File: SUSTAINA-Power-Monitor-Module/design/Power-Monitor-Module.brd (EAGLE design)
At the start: 20.3 x 12.7 mm, 25 parts, among them IC1 INA226, P1 2X5P, P2 2X5P, P3 1X4P

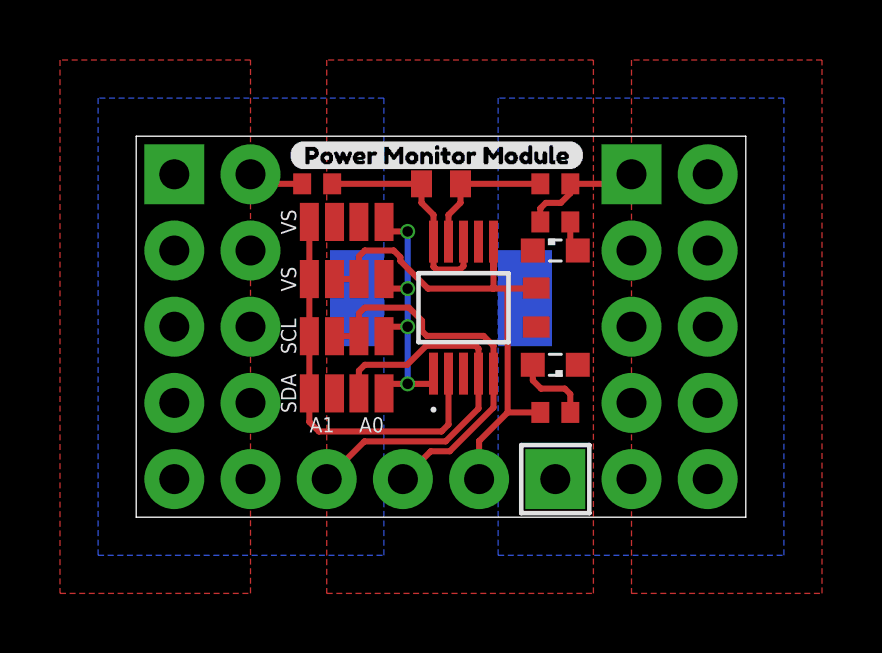
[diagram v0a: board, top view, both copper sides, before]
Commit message: Corrected the silk printing and via processing method
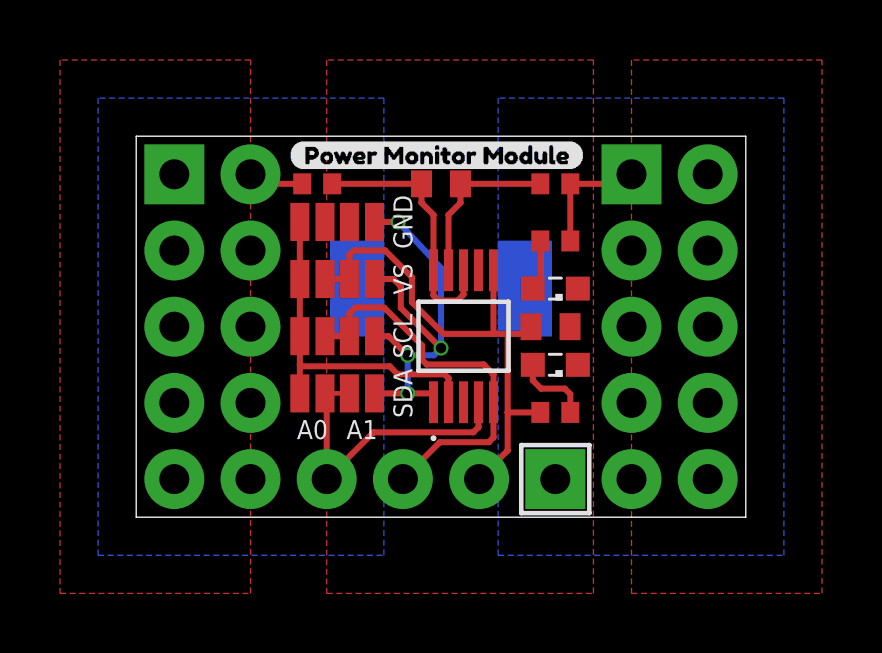
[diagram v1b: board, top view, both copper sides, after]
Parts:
- U$5: device buzzard_labels:DESIGNED_BY_MASATO_KUBOTERA_ON_MAY_1-0.0225 -> buzzard_labels:DESIGNED_BY_MASATO_KUBOTERA_ON_MAY_25-0.0225
- moved LED1 1.27 mm to (3.81, 1.27), turned to 180 degrees
- moved IC1 0.95 mm to (0.75, -0.32)
- moved C2 0.79 mm to (3.65, 0.00), turned to 0 degrees
- moved R4 0.64 mm to (3.81, 2.86), turned to 0 degrees
- moved R1 0.32 mm to (0.00, 1.27)
- moved JP1 0.32 mm to (-4.29, 3.49)
- moved JP2 0.32 mm to (-4.29, 1.59)
- moved JP3 0.32 mm to (-4.29, -2.22)
- moved JP4 0.32 mm to (-4.29, -0.32)
- moved JP5 0.32 mm to (-2.64, 3.49)
- moved JP6 0.32 mm to (-2.64, 1.59)
- moved JP7 0.32 mm to (-2.64, -2.22)
- moved JP8 0.32 mm to (-2.64, -0.32)
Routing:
- net A1: track 10.7 -> 15.3 mm
- net SDA: track 13.2 -> 10.3 mm
- net A0: track 13.2 -> 11.7 mm
- net IN+: track 7.81 -> 8.83 mm
- net IN-: track 4.75 -> 5.71 mm
- net VS: track 19.0 -> 18.1 mm
- net LED1_: track 1.06 -> 1.69 mm
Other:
- board text added: "GND"
